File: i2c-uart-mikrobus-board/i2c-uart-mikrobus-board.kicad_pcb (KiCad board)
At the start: 2 copper layers, 25.4 x 42.9 mm, 9 parts, among them J1 mikroBUS_Board_L, J2 mikroBUS_Board_R, J3 Conn_02x08_Odd_Even, SW1 SW_Rotary4, SW2 SW_Rotary4, U1 SC16IS740IPW, Y1 1.8432MHz

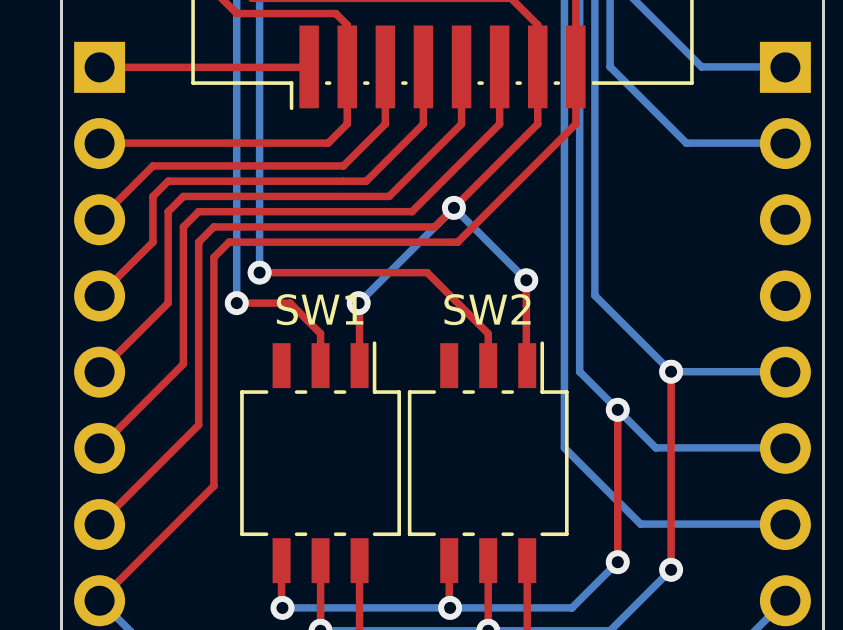
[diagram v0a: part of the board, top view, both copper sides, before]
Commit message: i2c-uart: fix rotary switch orientation
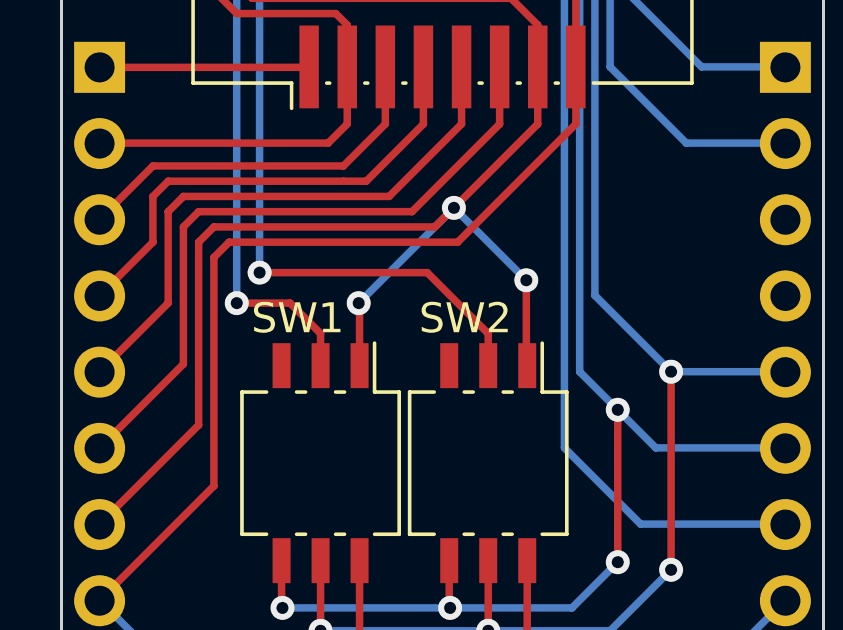
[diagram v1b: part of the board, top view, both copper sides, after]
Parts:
- turned SW1 to -90 degrees
- turned SW2 to -90 degrees

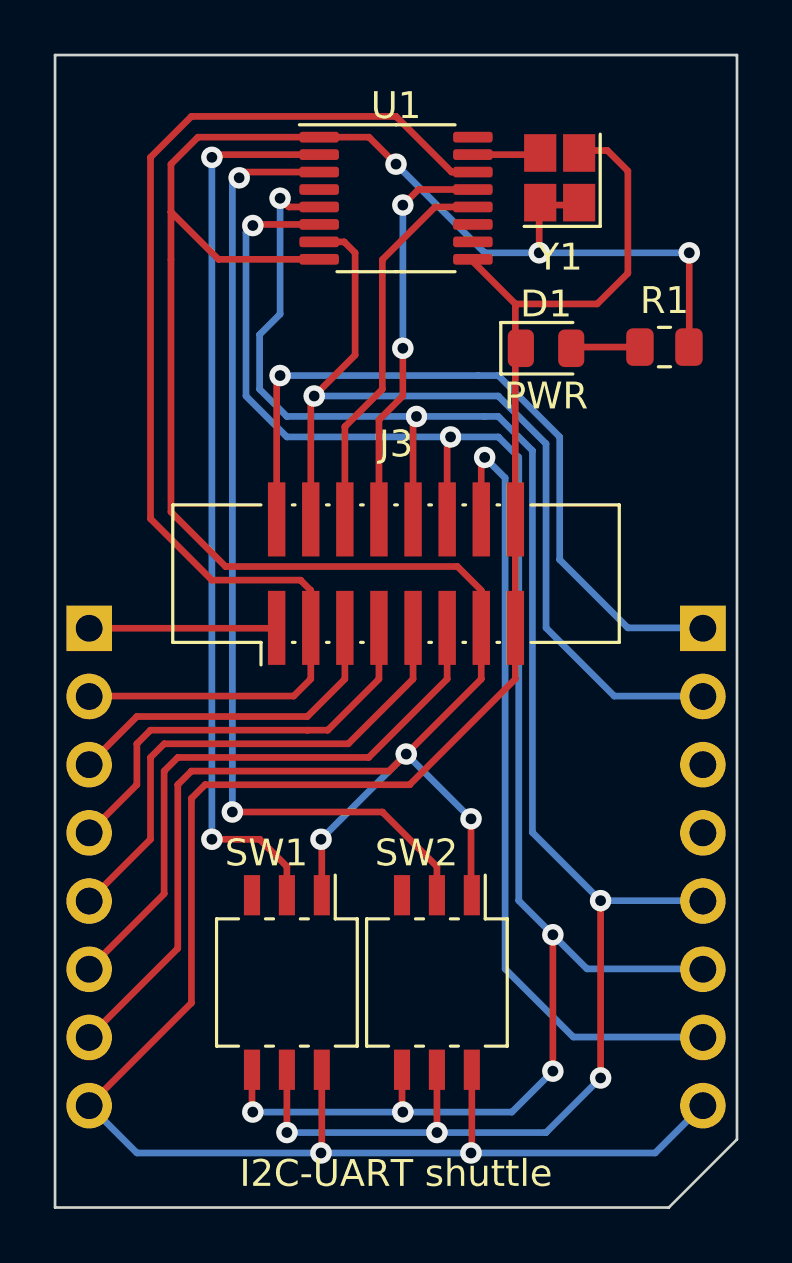
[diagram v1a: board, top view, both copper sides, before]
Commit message: i2c-uart: center Shuttle pin header footprint
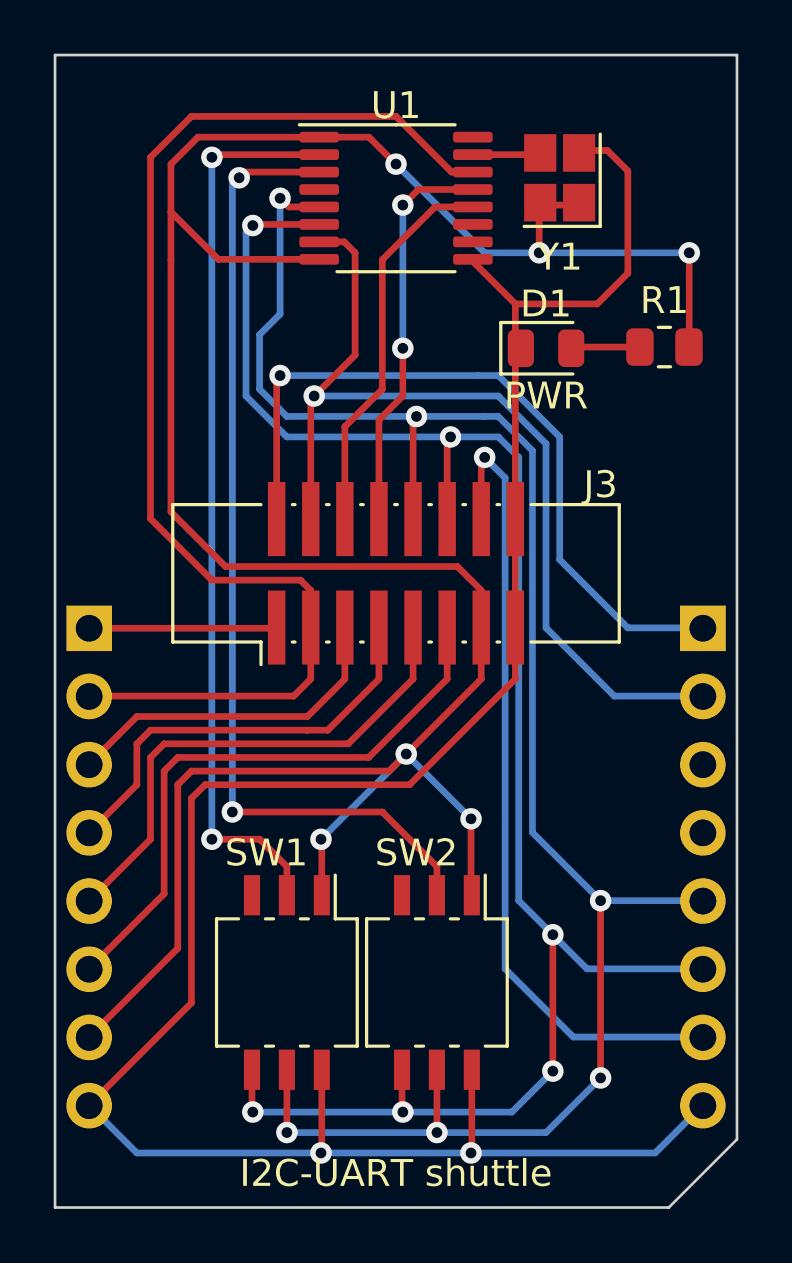
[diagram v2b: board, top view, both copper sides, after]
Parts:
- moved J3 4.89 mm to (38.1, 58.9)
